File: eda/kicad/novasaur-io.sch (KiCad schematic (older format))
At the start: 81 parts, among them J1 POWER IN, J10 EXPANSION, J3 AUDIO OUT, J4 KEYBOARD, J5 GPU OUT, J5 SERIAL, J6 DISPLAY, J7 EXPANSION, J8 EXPANSION, J9 EXPANSION, Q1 2N3904, Q2 2N3904, Q3 2N3904, SW1 POWER, SW2 RESET, U1 74F86, U3 74F11, U38 CD4053, U39 MAX232, U4 74F32, U40 NJM4580, U41 MCP1827S, U42 MCP1700, U6 74F139, U7 74F139

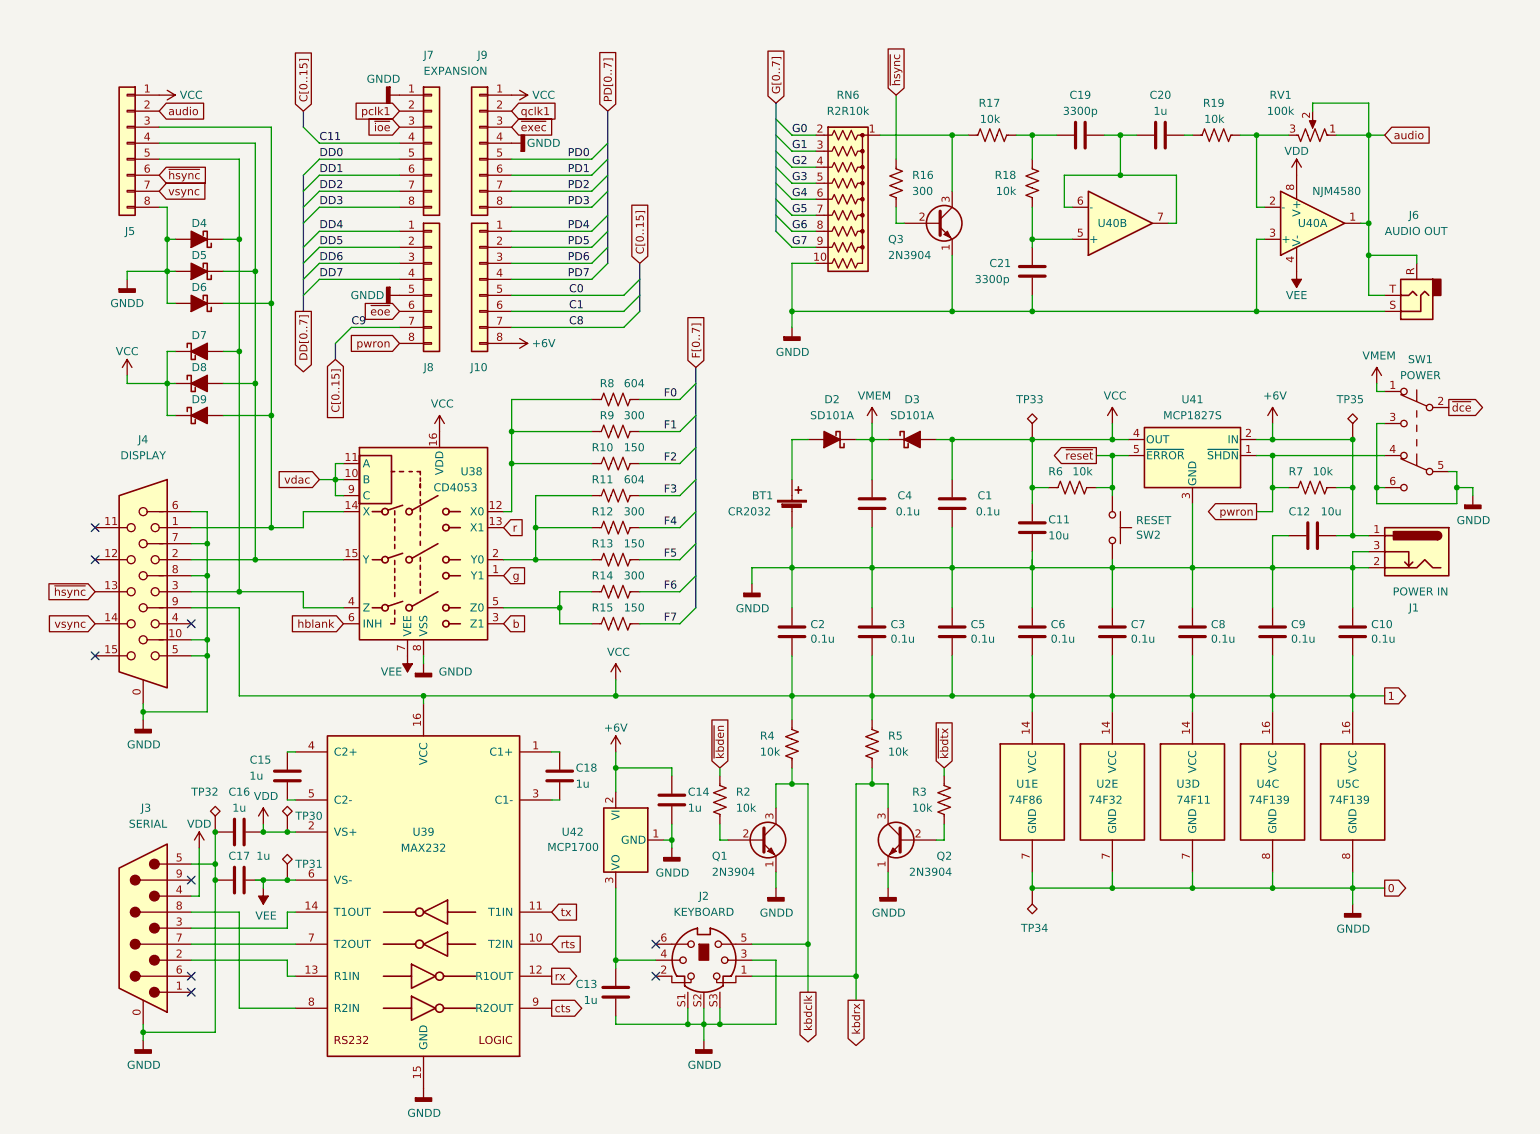
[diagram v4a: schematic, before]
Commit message: roll back to new 6v reg
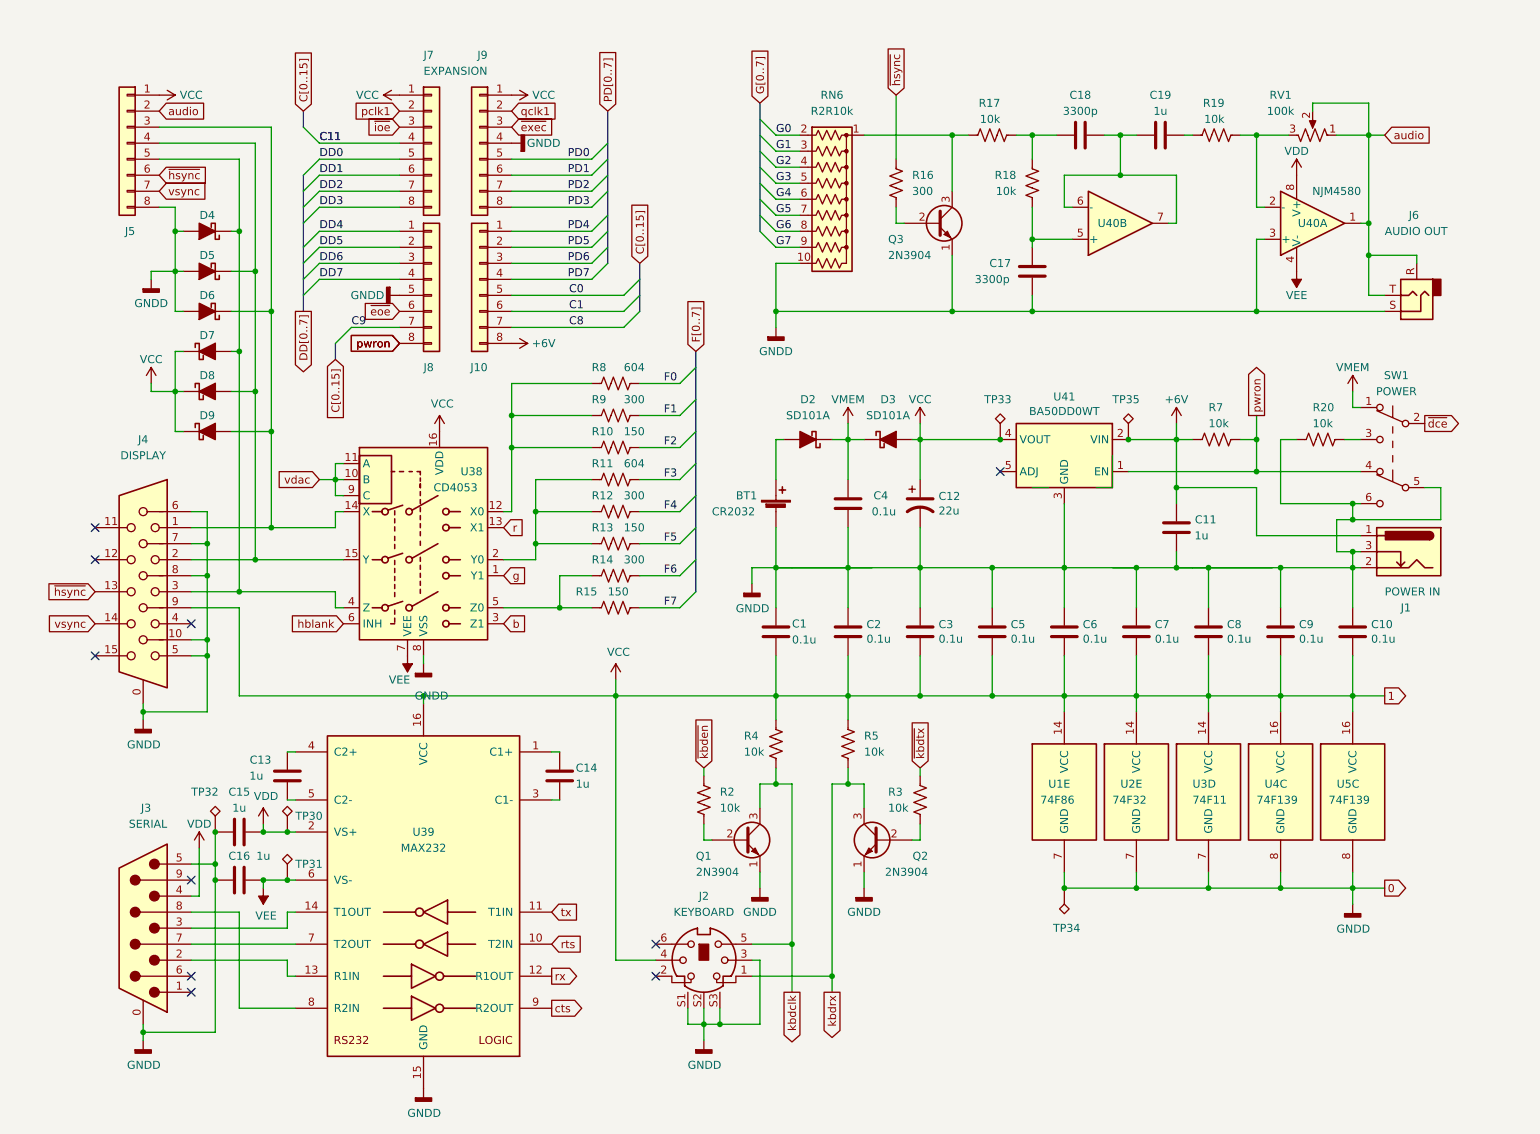
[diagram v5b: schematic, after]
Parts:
- removed C11, C12: 10u, Capacitor_THT:C_Disc_D5.0mm_W2.5mm_P2.50mm, symbol Device:C
- removed C14: 1u, Capacitor_THT:C_Disc_D5.1mm_W3.2mm_P5.00mm, symbol Device:C
- removed R6: 10k, Resistor_THT:R_Axial_DIN0204_L3.6mm_D1.6mm_P7.62mm_Horizontal, symbol Device:R_US
- removed SW2: RESET, Button_Switch_THT:SW_DIP_SPSTx01_Slide_6.7x4.1mm_W7.62mm_P2.54mm_LowProfile, symbol Switch:SW_Push
- removed U41: MCP1827S, Package_TO_SOT_THT:TO-220-5_P3.4x3.8mm_StaggerOdd_Lead7.13mm_TabDown, symbol Regulator_Linear:LP3963-3.3
- removed U42: MCP1700, Package_TO_SOT_THT:TO-92_HandSolder, symbol Regulator_Linear:MCP1700-5002E_TO92
- added C12: 22u, Capacitor_THT:CP_Radial_Tantal_D6.0mm_P5.00mm, symbol Device:CP1
- added R20: 10k, Resistor_THT:R_Axial_DIN0204_L3.6mm_D1.6mm_P7.62mm_Horizontal, symbol Device:R_US
- added U41: BA50DD0WT, Package_TO_SOT_THT:TO-220-5_Vertical, symbol Regulator_Linear:MIC29302WT
- renumbered C13 to C11, C19 to C18
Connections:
- net +6V: now also C11.2, R7.2, U41.2 (VIN); no longer R7.1
- net GNDD: now also C11.1, C12.2, R20.2, U41.3 (GND); no longer C11.2, J7.1 (Pin_1), SW1.3 (C)
- net VCC: now also J4.4, J7.1 (Pin_1), C12.1, U41.4 (VOUT)
- net pwron: now also R7.1, U41.1 (EN); no longer R7.2
- new net: R20.1, SW1.3 (C)
- no-connect marks 9 -> 10
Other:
- moved on the sheet: BT1, C1, C11, C2, C3, C4, C5, C6, C7, C8, C9, D2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
